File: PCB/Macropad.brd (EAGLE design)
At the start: 127 x 133.3 mm, 74 parts, among them IC1 LM2937, U1 EC11E09244AQ, X1 ZX62D-B-5PA8

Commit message: Updated power lines
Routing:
- net +3V3: track 230.9 -> 224.2 mm
- net D-: track 34.5 -> 37.1 mm
- net D+: track 34.4 -> 36.8 mm
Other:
- board text added: "EE445L Final Project WA, AC, JG, NC TA: MY Macropad"

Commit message: updated some routing
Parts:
- moved C18 0.20 mm to (113.8, 118.9)
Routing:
- net ROW_5: track 308.1 -> 187.8 mm
- net ROW_4: track 158.4 -> 166.6 mm
- net ROW_3: track 135.6 -> 142.7 mm
- net ROW_0: track 117.2 -> 121.5 mm
- net PF2: track 89.9 -> 92.7 mm
- net COLUMN_0: track 270.5 -> 271.3 mm
- net WAKE: track 20.9 -> 21.6 mm
- net ST7735_TFT_CS: track 96.6 -> 97.2 mm
- net ROW_1: track 110.1 -> 110.7 mm
- net COLUMN_2: track 205.1 -> 205.7 mm

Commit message: Added Matthew's urgent updates
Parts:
- added C13: 0.1uf, EE445L:CAP100MIL
- added JP1: (no value), EE445L:1X04
- added U2: TPD2E001DRLR, TPD2E001DRLR:SOT50P160X60-5N
- C1: value 0.01uf -> 10uF
- C2, C4: value 0.1uf -> 0.1uF
- C3, C5: value 0.01uf -> 0.1uF
- C9: value 0.1uf -> 1.0uf
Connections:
- net +5V: now also C13.1, JP1.1, U2.1
- net D+: now also JP1.2, U2.3
- net D-: now also JP1.3, U2.5
- net GND: now also C13.2, JP1.4, U2.4
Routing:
- net GND: track 313.5 -> 328.0 mm
- net +5V: track 49.6 -> 63.4 mm, vias 1 -> 2
- net D-: track 37.0 -> 47.6 mm
- net D+: track 36.8 -> 39.7 mm, vias 0 -> 1

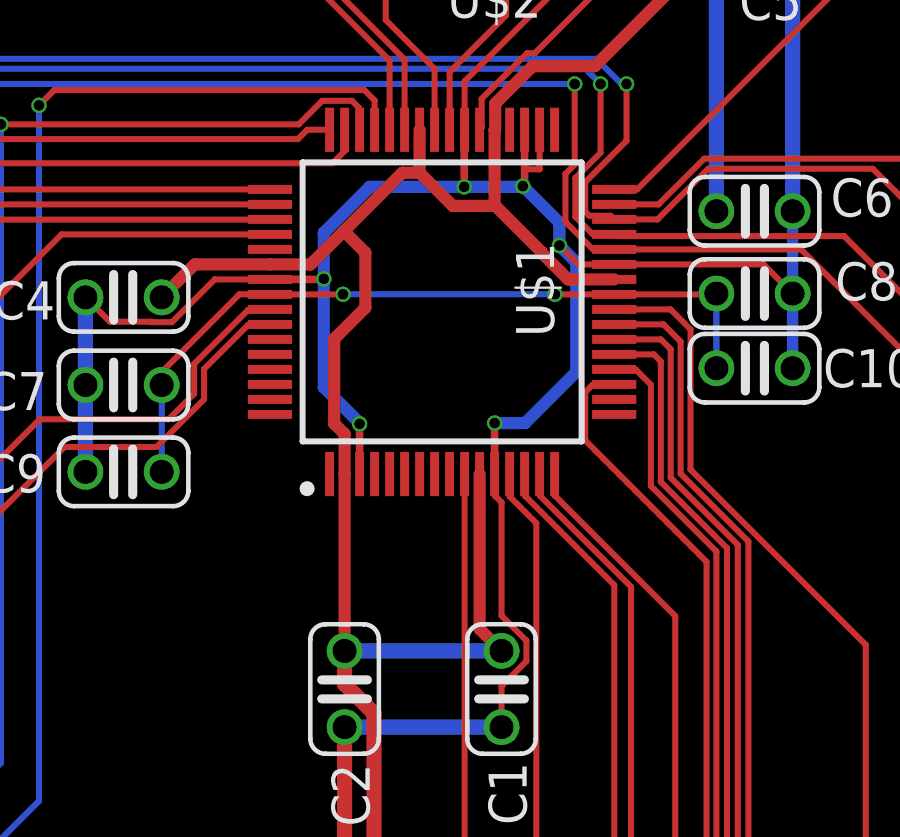
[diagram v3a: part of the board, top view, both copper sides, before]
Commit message: Fixed ground loop
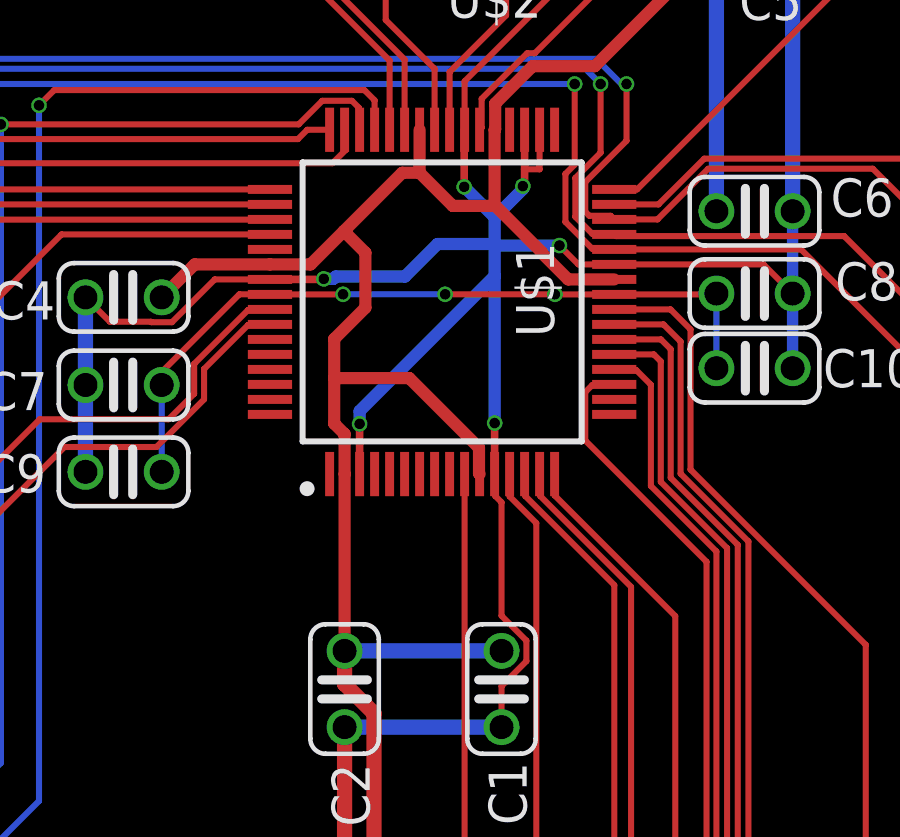
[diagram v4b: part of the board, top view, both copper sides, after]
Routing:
- net VDDC: vias 2 -> 3
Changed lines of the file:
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@@
 <via x="107.2642" y="89.7382" extent="1-16" drill="0.35"/>
 <wire x1="102.7616" y1="88.0388" x2="102.7616" y2="89.7128" width="0.254" layer="1"/>
-<wire x1="101.5678" y1="94.5456" x2="101.5678" y2="90.932" width="0.4064" layer="16"/>
-<wire x1="101.5678" y1="90.932" x2="102.7616" y2="89.7382" width="0.4064" layer="16"/>
 <wire x1="102.7616" y1="89.7128" x2="102.7616" y2="89.7382" width="0.2032" layer="16"/>
 <wire x1="101.549" y1="94.5268" x2="99.7736" y2="94.5268" width="0.254" layer="1"/>
@@
 <wire x1="117.1956" y1="94.403253125" x2="117.11813125" y2="94.480721875" width="0.381" layer="16"/>
 <wire x1="117.1956" y1="94.0562" x2="117.1956" y2="96.7994" width="0.381" layer="16"/>
-<wire x1="109.4232" y1="95.6564" x2="109.982" y2="95.0976" width="0.4064" layer="16"/>
-<wire x1="109.982" y1="95.0976" x2="109.982" y2="91.44" width="0.4064" layer="16"/>
-<wire x1="107.2642" y1="89.7382" x2="108.2802" y2="89.7382" width="0.4064" layer="16"/>
-<wire x1="109.982" y1="91.44" x2="108.2802" y2="89.7382" width="0.4064" layer="16"/>
 <wire x1="107.2616" y1="88.0388" x2="107.2616" y2="89.7356" width="0.254" layer="1"/>
 <wire x1="107.2616" y1="89.7356" x2="107.2642" y2="89.7382" width="0.2032" layer="1"/>
-<wire x1="101.5678" y1="94.5456" x2="101.5678" y2="96.0814" width="0.4064" layer="16"/>
-<wire x1="103.0986" y1="97.6122" x2="106.2482" y2="97.6122" width="0.4064" layer="16"/>
-<wire x1="103.0986" y1="97.6122" x2="101.5678" y2="96.0814" width="0.4064" layer="16"/>
 <contactref element="C16" pad="-"/>
 <contactref element="IC1" pad="2"/>
@@
 <wire x1="108.2616" y1="99.5148" x2="108.2616" y2="98.1964" width="0.254" layer="1"/>
 <wire x1="108.2616" y1="98.1964" x2="108.2616" y2="97.6952" width="0.254" layer="1"/>
-<wire x1="108.2616" y1="97.6952" x2="108.204" y2="97.6376" width="0.254" layer="1"/>
 <via x="108.204" y="97.6376" extent="1-16" drill="0.35"/>
 <wire x1="108.7616" y1="99.5148" x2="108.7616" y2="98.1964" width="0.2032" layer="1"/>
@@
 <wire x1="107.4928" y1="87.0968125" x2="107.4928" y2="83.31541875" width="0.2032" layer="1"/>
 <wire x1="107.4928" y1="83.31541875" x2="108.3214" y2="82.48681875" width="0.2032" layer="1"/>
-<wire x1="108.204" y1="97.6376" x2="109.4232" y2="96.4184" width="0.4064" layer="16"/>
-<wire x1="109.4232" y1="96.4184" x2="109.4232" y2="95.6564" width="0.4064" layer="16"/>
-<wire x1="106.2482" y1="97.6122" x2="108.1786" y2="97.6122" width="0.4064" layer="16"/>
 <wire x1="108.1786" y1="97.6122" x2="108.204" y2="97.6376" width="0.4064" layer="16"/>
 <wire x1="116.225" y1="95.0268" x2="117.1956" y2="94.0562" width="0.2032" layer="1"/>
@@
 <wire x1="111.9165" y1="126.1816" x2="111.9435" y2="126.2086" width="0.508" layer="1"/>
 <wire x1="111.9435" y1="126.2086" x2="112.80908125" y2="126.2086" width="0.508" layer="1"/>
+<wire x1="106.2482" y1="97.6122" x2="107.2642" y2="96.5962" width="0.4064" layer="16"/>
+<wire x1="107.2642" y1="96.5962" x2="107.2642" y2="95.7072" width="0.4064" layer="16"/>
+<wire x1="107.2642" y1="95.7072" x2="107.2642" y2="94.6404" width="0.4064" layer="16"/>
+<wire x1="107.2642" y1="94.6404" x2="107.2642" y2="89.7382" width="0.4064" layer="16"/>
+<wire x1="102.7616" y1="89.7128" x2="102.7616" y2="90.1378" width="0.4064" layer="16"/>
+<wire x1="102.7616" y1="90.1378" x2="107.2642" y2="94.6404" width="0.4064" layer="16"/>
+<wire x1="108.204" y1="97.6376" x2="108.204" y2="97.536" width="0.4064" layer="16"/>
+<wire x1="108.204" y1="97.536" x2="107.2642" y2="96.5962" width="0.4064" layer="16"/>
+<wire x1="109.4232" y1="95.6564" x2="107.315" y2="95.6564" width="0.4064" layer="16"/>
+<wire x1="107.315" y1="95.6564" x2="107.2642" y2="95.7072" width="0.4064" layer="16"/>
+<wire x1="101.5678" y1="94.5456" x2="101.88619375" y2="94.5456" width="0.4064" layer="16"/>
+<wire x1="101.88619375" y1="94.5456" x2="101.96409375" y2="94.6235" width="0.4064" layer="16"/>
+<wire x1="101.96409375" y1="94.6235" x2="104.2755" y2="94.6235" width="0.4064" layer="16"/>
+<wire x1="105.3592" y1="95.7072" x2="107.2642" y2="95.7072" width="0.4064" layer="16"/>
+<wire x1="104.2755" y1="94.6235" x2="105.3592" y2="95.7072" width="0.4064" layer="16"/>
+<wire x1="108.204" y1="97.6376" x2="108.2616" y2="97.6952" width="0" layer="19" extent="1-1"/>
 </signal>
 <signal name="+3V3">
@@
 <wire x1="102.2616" y1="88.0388" x2="102.2616" y2="89.37459375" width="0.4064" layer="1"/>
 <wire x1="102.2616" y1="89.37459375" x2="101.9149" y2="89.72129375" width="0.4064" layer="1"/>
-<wire x1="101.9149" y1="89.72129375" x2="101.9149" y2="92.54229375" width="0.4064" layer="1"/>
+<wire x1="101.9149" y1="89.72129375" x2="101.9149" y2="91.2368" width="0.4064" layer="1"/>
+<wire x1="101.9149" y1="91.2368" x2="101.9149" y2="92.54229375" width="0.4064" layer="1"/>
 <wire x1="101.9149" y1="92.54229375" x2="102.9547" y2="93.58209375" width="0.4064" layer="1"/>
 <wire x1="102.9547" y1="93.58209375" x2="102.9547" y2="95.4193" width="0.4064" layer="1"/>
@@
 <wire x1="108.8305" y1="95.41089375" x2="109.71459375" y2="94.5268" width="0.4064" layer="1"/>
 <wire x1="109.71459375" y1="94.5268" x2="111.2496" y2="94.5268" width="0.4064" layer="1"/>
-<wire x1="106.7616" y1="88.0388" x2="106.7616" y2="82.8748" width="0.4064" layer="1"/>
-<wire x1="106.7616" y1="82.8748" x2="107.4928" y2="82.1436" width="0.4064" layer="1"/>
 <wire x1="104.7616" y1="99.5148" x2="104.7616" y2="98.0828" width="0.4064" layer="1"/>
 <wire x1="104.7616" y1="98.0828" x2="105.8672" y2="96.9772" width="0.4064" layer="1"/>
 <wire x1="102.2376375" y1="96.1363625" x2="104.184075" y2="98.0828" width="0.4064" layer="1"/>
 <wire x1="104.184075" y1="98.0828" x2="104.7616" y2="98.0828" width="0.4064" layer="1"/>
+<wire x1="106.7616" y1="88.0388" x2="106.7418" y2="88.0586" width="0.4064" layer="1"/>
+<wire x1="106.7418" y1="88.0586" x2="106.7418" y2="88.913075" width="0.4064" layer="1"/>
+<wire x1="106.7418" y1="88.913075" x2="104.418075" y2="91.2368" width="0.4064" layer="1"/>
+<wire x1="104.418075" y1="91.2368" x2="101.9149" y2="91.2368" width="0.4064" layer="1"/>
 </signal>
 <signal name="VDDC">
@@
 <wire x1="102.2056" y1="94.0268" x2="102.2096" y2="94.0308" width="0.2032" layer="1"/>
 <via x="102.2096" y="94.0308" extent="1-16" drill="0.35"/>
-<wire x1="102.2096" y1="94.0308" x2="109.2708" y2="94.0308" width="0.2032" layer="16"/>
 <wire x1="99.7736" y1="94.0268" x2="102.2056" y2="94.0268" width="0.2032" layer="1"/>
 <wire x1="98.7552" y1="94.0308" x2="96.1644" y2="91.44" width="0.2032" layer="1"/>
@@
 <wire x1="114.6556" y1="94.0562" x2="114.6556" y2="91.567" width="0.2032" layer="16"/>
 <wire x1="111.2496" y1="94.0268" x2="114.644865625" y2="94.0268" width="0.2032" layer="1"/>
+<via x="105.6132" y="94.0308" extent="1-16" drill="0.35"/>
+<wire x1="102.2096" y1="94.0308" x2="105.6132" y2="94.0308" width="0.2032" layer="16"/>
+<wire x1="105.6132" y1="94.0308" x2="109.2668" y2="94.0308" width="0.2032" layer="1"/>
+<wire x1="109.2668" y1="94.0308" x2="109.2708" y2="94.0268" width="0.2032" layer="1"/>
 </signal>
 <signal name="+5V">

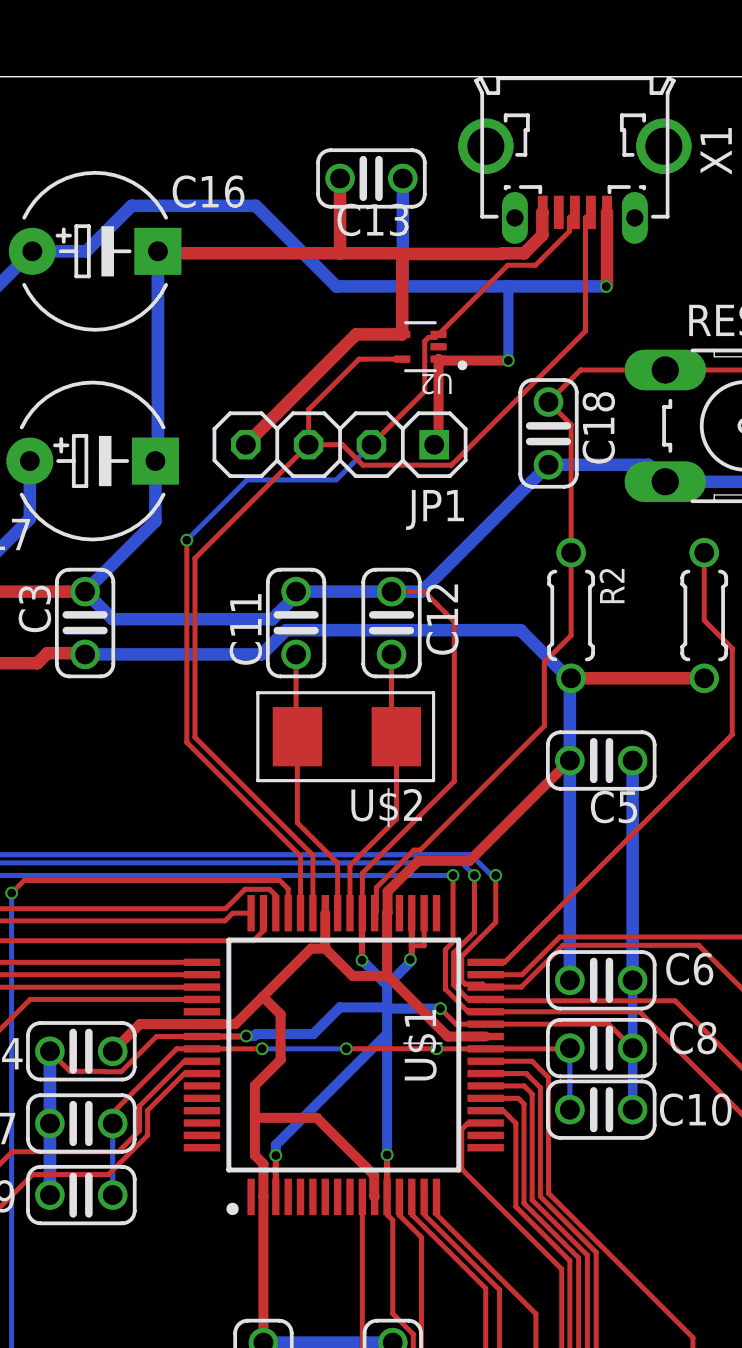
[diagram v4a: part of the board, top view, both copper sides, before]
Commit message: Changed TVS part
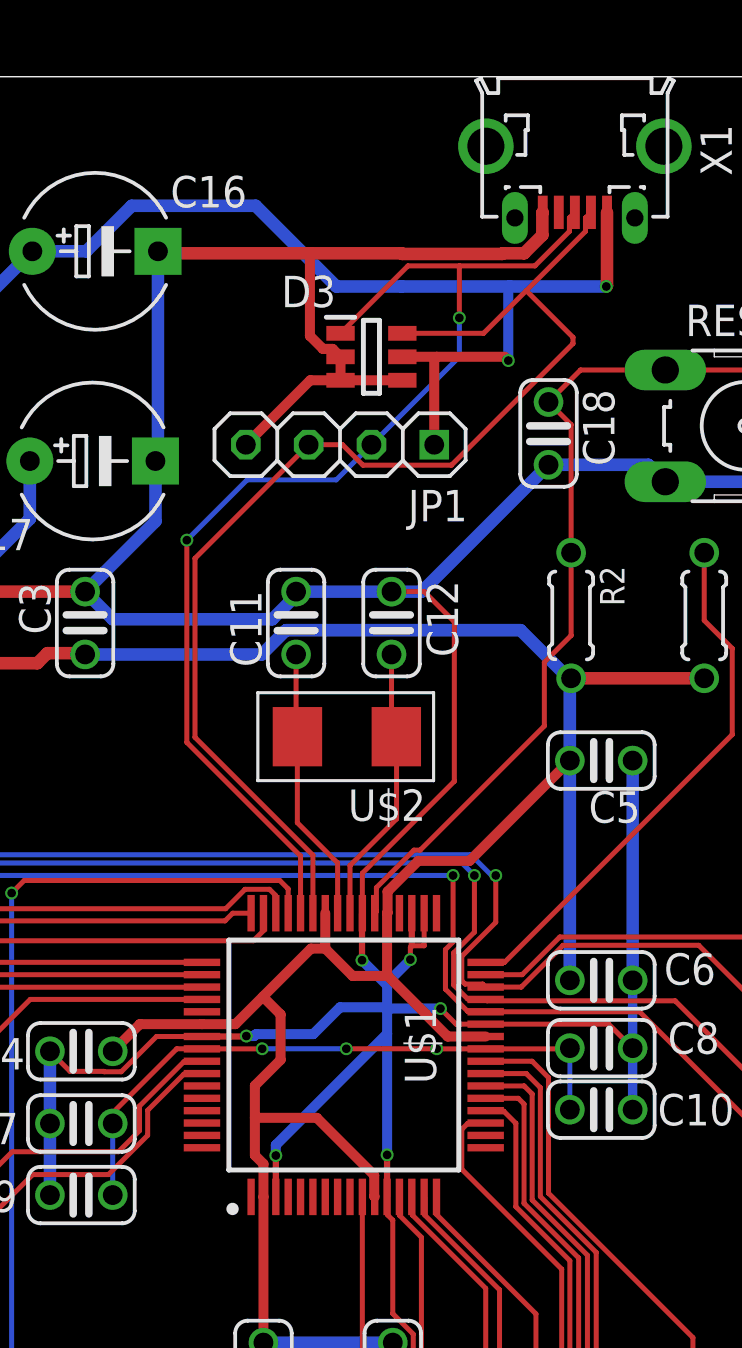
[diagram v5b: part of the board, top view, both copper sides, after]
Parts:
- removed C13: 0.1uf, EE445L:CAP100MIL
- removed U2: TPD2E001DRLR, TPD2E001DRLR:SOT50P160X60-5N
- added D3: SRV05-4.TCT, SRV05-4.TCT:SOT95P280X145-6N
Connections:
- net +5V: now also D3.5; no longer C13.1, U2.1
- net D+: now also D3.1; no longer U2.3
- net D-: now also D3.6; no longer U2.5
- net GND: now also D3.2, D3.3, D3.4; no longer C13.2, U2.4
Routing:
- net D+: track 39.7 -> 46.6 mm, vias 1 -> 2
- net +5V: track 63.4 -> 60.5 mm
- net D-: track 47.6 -> 48.8 mm
- net GND: track 328.4 -> 327.2 mm

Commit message: Added not urgent but recommended updates
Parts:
- moved U$6 61.3 mm to (116.5, 62.4), turned to 270 degrees
- moved C22 32.3 mm to (90.9, 69.2)
- moved C23 32.3 mm to (98.3, 69.2)
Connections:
- net GND: now also X1.4
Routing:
- net ST7735_RST: track 117.0 -> 36.2 mm
- net ST7735_DC: track 113.4 -> 36.3 mm
- net ST7735_CARD_CS: track 83.6 -> 26.9 mm
- net +3V3: track 225.0 -> 169.2 mm
- net ST7735_MOSI: track 103.0 -> 47.6 mm, vias 0 -> 1
- net ST7735_TFT_CS: track 97.2 -> 43.8 mm, vias 0 -> 1
- net ST7735_SCK: track 89.3 -> 45.3 mm, vias 0 -> 1
- net GND: track 327.2 -> 283.3 mm
- net ST7735_MISO: track 89.3 -> 48.2 mm, vias 0 -> 1
